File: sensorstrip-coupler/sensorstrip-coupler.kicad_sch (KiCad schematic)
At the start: 2 parts, among them J1 Conn_01x02_MountingPin, J2 Conn_01x02_MountingPin

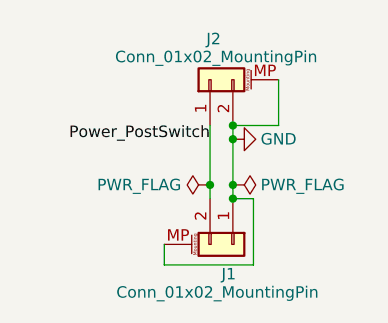
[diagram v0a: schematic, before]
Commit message: Cleanup in preparation for push
Update project files to KiCad 7 format
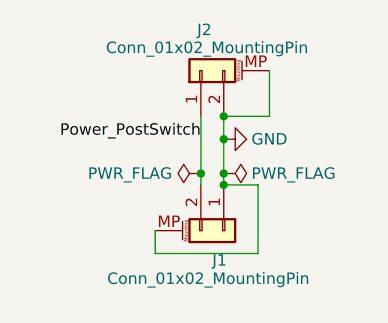
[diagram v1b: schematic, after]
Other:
- moved on the sheet: J1, J2
